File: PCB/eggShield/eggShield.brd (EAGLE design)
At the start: 100 x 80 mm, 35 parts, among them IC10 MCP601OT, IC3 LM339D, IC6 MCP601OT, IC7 MCP601OT

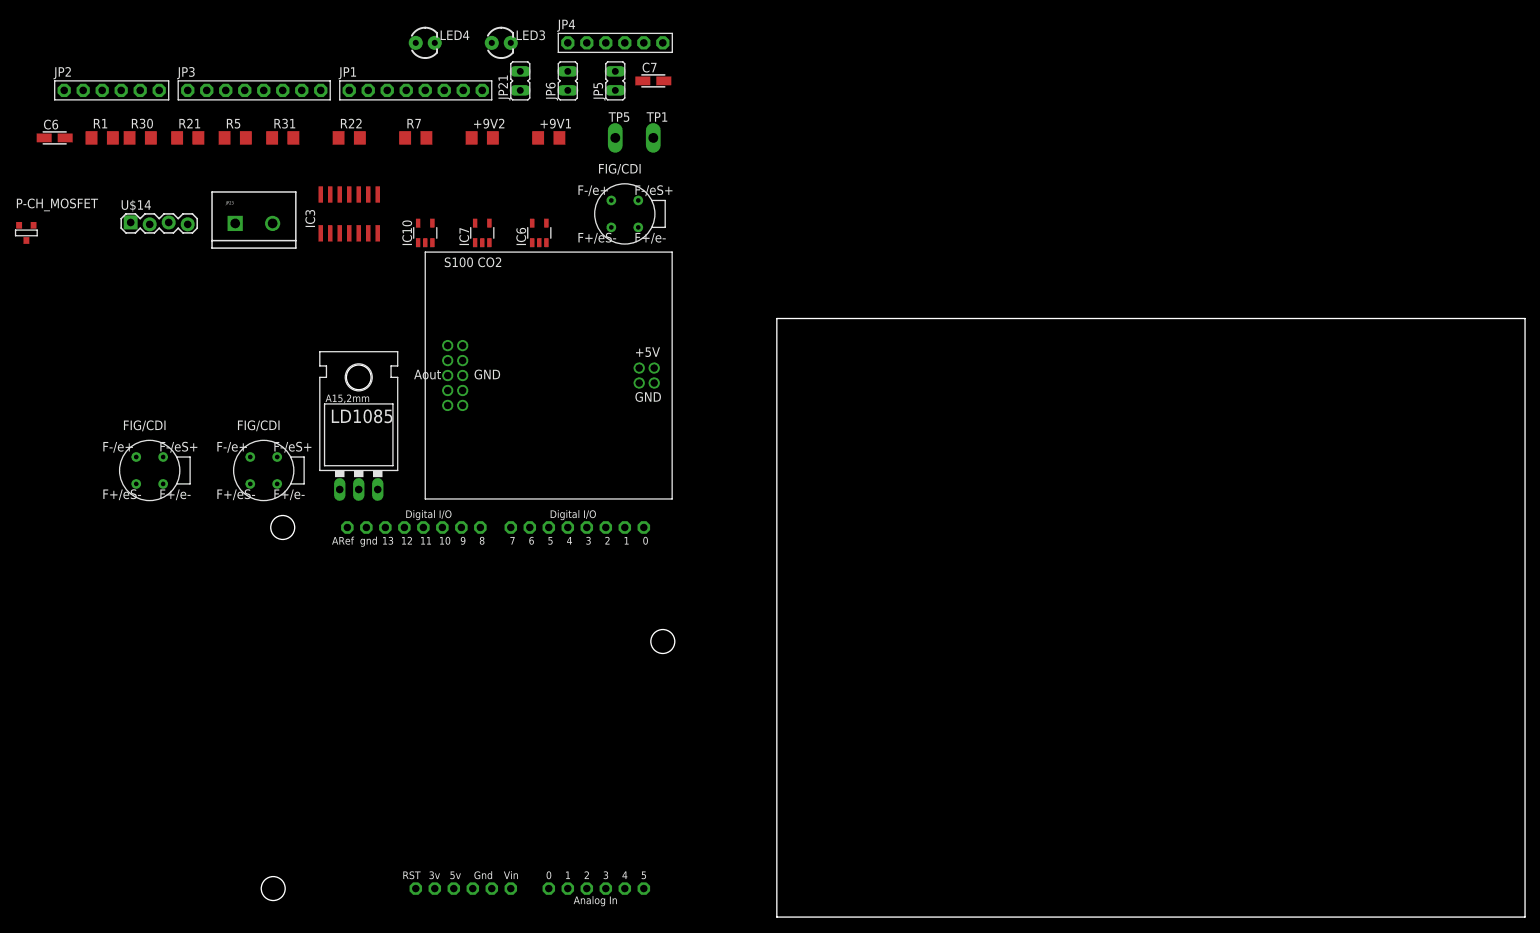
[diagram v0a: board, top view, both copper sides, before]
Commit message: added .brd, cleaned up
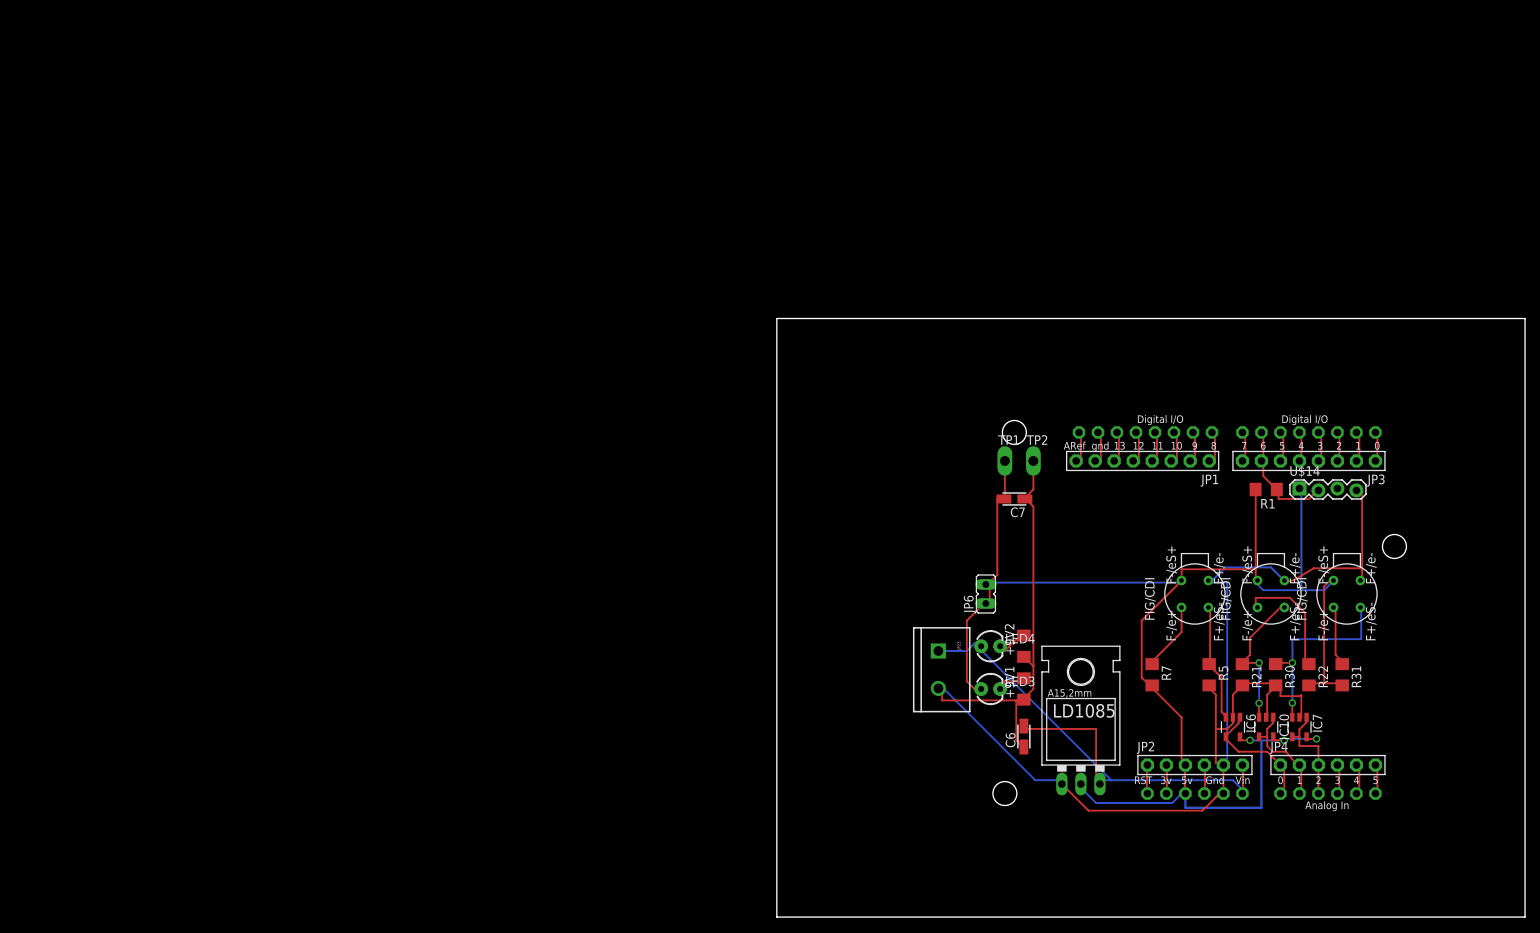
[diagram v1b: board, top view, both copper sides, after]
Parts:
- removed IC3: LM339D, linear:SO14
- removed JP21, JP5: (no value), jumper:JP1
- removed P-CH_MOSFET: ZXM61P02FCT, zetex:SOT-23
- removed TP5: TPPAD1-13Y, testpad:P1-13Y
- removed U$6: S100CO2, ricardo:S100CO2
- added TP2: TPPAD1-13Y, testpad:P1-13Y
- moved JP2 170.6 mm to (55.9, 20.3)
- moved R30 167.9 mm to (66.7, 32.4), turned to 270 degrees
- moved R1 162.5 mm to (65.4, 57.1), turned to 180 degrees
- moved U$9 160.9 mm to (76.2, 43.2), turned to 90 degrees
- moved U$14 160.2 mm to (69.8, 57.1)
- moved R31 158.7 mm to (75.6, 32.4), turned to 270 degrees
- moved R21 158.2 mm to (62.2, 32.4), turned to 270 degrees
- moved C6 152.3 mm to (33.0, 24.1), turned to 90 degrees
- moved JP3 149.4 mm to (71.1, 61.0), turned to 180 degrees
- moved R5 148.6 mm to (57.8, 32.4), turned to 270 degrees
- moved R22 147.0 mm to (71.1, 32.4), turned to 270 degrees
- moved JP4 135.6 mm to (73.7, 20.3)
- moved IC10 130.4 mm to (65.4, 25.4), turned to 180 degrees
- moved IC7 127.6 mm to (69.8, 25.4), turned to 180 degrees
- moved NO2 125.6 mm to (55.9, 43.2), turned to 90 degrees
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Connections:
- removed net A5: JP21.2, U$6.AOUT
- removed net D5: P-CH_MOSFET.3
- removed net N$49: P-CH_MOSFET.2, U$6.+5V1, U$6.+5V2
- net +9V: no longer IC3.3, JP5.1, JP5.2
- net GND: now also TP2.TP; no longer IC3.12, JP21.1, TP5.TP, U$6.GND2, U$6.GND9
- net V+: no longer P-CH_MOSFET.1
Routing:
- net V+: track 0.00 -> 216.2 mm, vias 0 -> 3
- net GND: track 0.00 -> 207.8 mm
- net +9V: track 0.00 -> 73.7 mm
- net N$55: track 0.00 -> 26.3 mm, vias 0 -> 2
- net N$47: track 0.00 -> 21.0 mm, vias 0 -> 2
- net N$52: track 0.00 -> 16.8 mm
- net N$50: track 0.00 -> 16.0 mm
- net A3: track 0.00 -> 15.8 mm
- net N$38: track 0.00 -> 15.8 mm
- net N$48: track 0.00 -> 14.6 mm
- net N$9: track 0.00 -> 14.1 mm
- net N$43: track 0.00 -> 9.17 mm
- net N$45: track 0.00 -> 8.03 mm
- net N$29: track 0.00 -> 4.71 mm
- net N$27: track 0.00 -> 4.71 mm
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
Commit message: cleaned board
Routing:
- net N$9: track 14.1 -> 12.6 mm
- net N$52: track 16.8 -> 17.8 mm
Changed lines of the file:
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@@
 <wire x1="22.352" y1="30.48" x2="21.59" y2="30.56" width="0.254" layer="16"/>
 <wire x1="37.592" y1="18.288" x2="38.1" y2="17.78" width="0.254" layer="16"/>
-<wire x1="56.896" y1="14.224" x2="58.674" y2="16.002" width="0.254" layer="1"/>
-<wire x1="58.674" y1="16.002" x2="58.928" y2="16.256" width="0.254" layer="1"/>
-<wire x1="41.656" y1="14.224" x2="56.896" y2="14.224" width="0.254" layer="1"/>
-<wire x1="38.1" y1="17.78" x2="41.656" y2="14.224" width="0.254" layer="1"/>
-<wire x1="58.928" y1="16.256" x2="59.69" y2="16.51" width="0.254" layer="1"/>
+<wire x1="59.436" y1="15.1765" x2="59.6265" y2="16.002" width="0.254" layer="1"/>
+<wire x1="59.6265" y1="16.002" x2="59.563" y2="16.256" width="0.254" layer="1"/>
+<wire x1="39.116" y1="15.1765" x2="59.436" y2="15.1765" width="0.254" layer="1"/>
+<wire x1="38.1" y1="17.78" x2="39.116" y2="15.1765" width="0.254" layer="1"/>
+<wire x1="59.563" y1="16.256" x2="59.69" y2="16.51" width="0.254" layer="1"/>
 <wire x1="60.96" y1="29.718" x2="60.96" y2="26.706" width="0.254" layer="1"/>
 <wire x1="61.722" y1="30.48" x2="60.96" y2="29.718" width="0.254" layer="1"/>
@@
 <wire x1="33.528" y1="29.718" x2="33.02" y2="29.058" width="0.254" layer="1"/>
 <wire x1="58.674" y1="29.718" x2="57.912" y2="30.48" width="0.254" layer="1"/>
-<wire x1="58.674" y1="16.002" x2="59.69" y2="16.51" width="0.254" layer="1"/>
+<wire x1="59.6265" y1="16.002" x2="59.69" y2="16.51" width="0.254" layer="1"/>
 <wire x1="59.69" y1="16.51" x2="59.69" y2="20.574" width="0.254" layer="1"/>
 <wire x1="59.69" y1="20.574" x2="59.436" y2="20.574" width="0.254" layer="1"/>
@@
 <wire x1="60.198" y1="24.384" x2="60.01" y2="24.094" width="0.254" layer="1"/>
 <wire x1="61.722" y1="26.67" x2="61.91" y2="26.706" width="0.254" layer="1"/>
-<wire x1="61.722" y1="22.098" x2="60.198" y2="23.622" width="0.254" layer="1"/>
-<wire x1="65.532" y1="22.098" x2="61.722" y2="22.098" width="0.254" layer="1"/>
-<wire x1="67.31" y1="20.32" x2="65.532" y2="22.098" width="0.254" layer="1"/>
+<wire x1="60.1345" y1="21.7805" x2="60.198" y2="23.622" width="0.254" layer="1"/>
+<wire x1="65.532" y1="21.7805" x2="60.1345" y2="21.7805" width="0.254" layer="1"/>
+<wire x1="67.31" y1="20.32" x2="65.532" y2="21.7805" width="0.254" layer="1"/>
 <wire x1="60.198" y1="23.622" x2="60.01" y2="24.094" width="0.254" layer="1"/>
 <wire x1="67.818" y1="19.812" x2="67.818" y2="16.764" width="0.254" layer="1"/>
@@
 <wire x1="65.532" y1="25.146" x2="66.294" y2="25.908" width="0.254" layer="1"/>
 <wire x1="65.532" y1="22.86" x2="65.532" y2="25.146" width="0.254" layer="1"/>
-<wire x1="66.294" y1="22.098" x2="65.532" y2="22.86" width="0.254" layer="1"/>
-<wire x1="68.072" y1="22.098" x2="66.294" y2="22.098" width="0.254" layer="1"/>
-<wire x1="69.342" y1="20.574" x2="68.072" y2="22.098" width="0.254" layer="1"/>
+<wire x1="65.659" y1="22.733" x2="65.532" y2="22.86" width="0.254" layer="1"/>
+<wire x1="67.437" y1="22.733" x2="65.659" y2="22.733" width="0.254" layer="1"/>
+<wire x1="69.977" y1="20.2565" x2="67.437" y2="22.733" width="0.254" layer="1"/>
 <wire x1="66.294" y1="26.67" x2="66.355" y2="26.706" width="0.254" layer="1"/>
-<wire x1="69.342" y1="20.574" x2="69.85" y2="20.32" width="0.254" layer="1"/>
+<wire x1="69.977" y1="20.2565" x2="69.85" y2="20.32" width="0.254" layer="1"/>
 <wire x1="70.104" y1="19.812" x2="70.104" y2="16.764" width="0.254" layer="1"/>
 <wire x1="70.104" y1="16.764" x2="69.85" y2="16.51" width="0.254" layer="1"/>
@@
 <wire x1="68.9" y1="24.094" x2="69.85" y2="24.094" width="0.254" layer="1"/>
 <wire x1="69.85" y1="24.094" x2="69.85" y2="22.86" width="0.254" layer="1"/>
-<wire x1="69.85" y1="22.86" x2="72.39" y2="22.86" width="0.254" layer="1"/>
-<wire x1="72.39" y1="22.86" x2="72.39" y2="20.32" width="0.254" layer="1"/>
+<wire x1="69.85" y1="22.86" x2="72.39" y2="20.32" width="0.254" layer="1"/>
 </signal>
 <signal name="N$10">

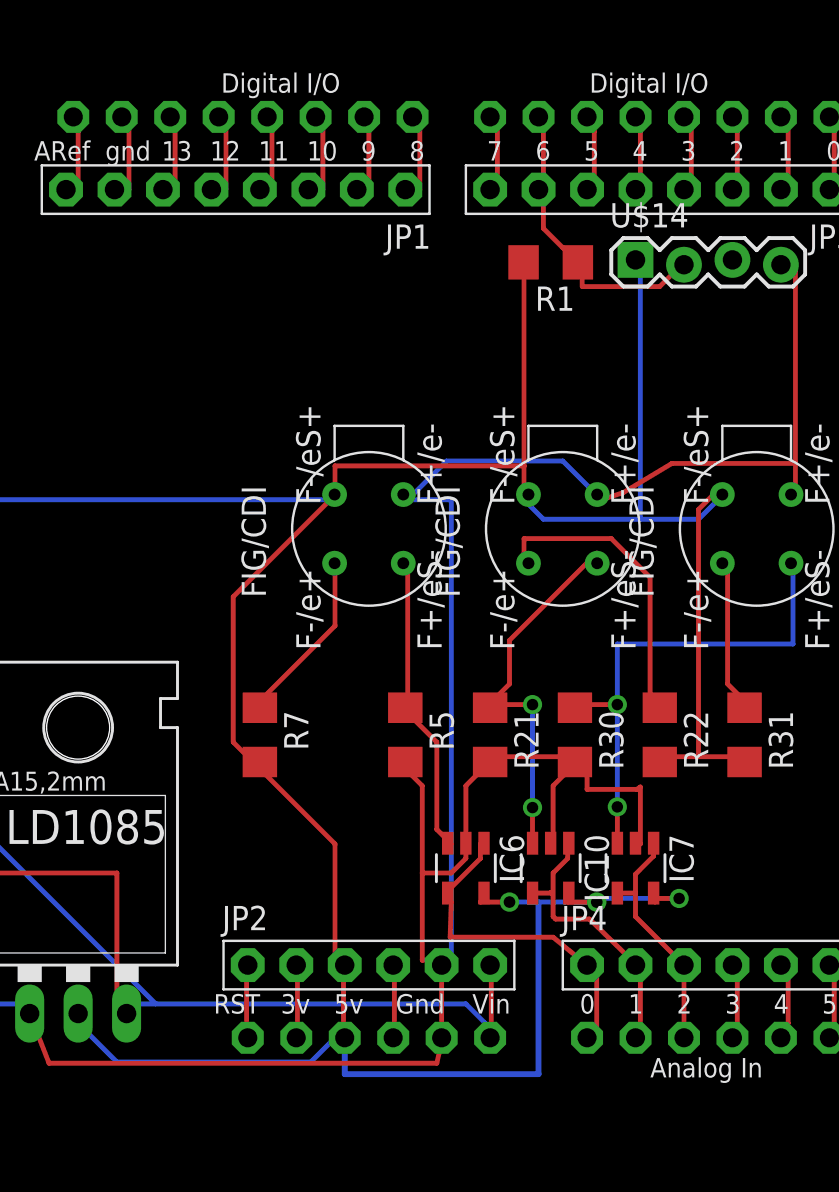
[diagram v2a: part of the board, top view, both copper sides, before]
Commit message: fixed RHT pin
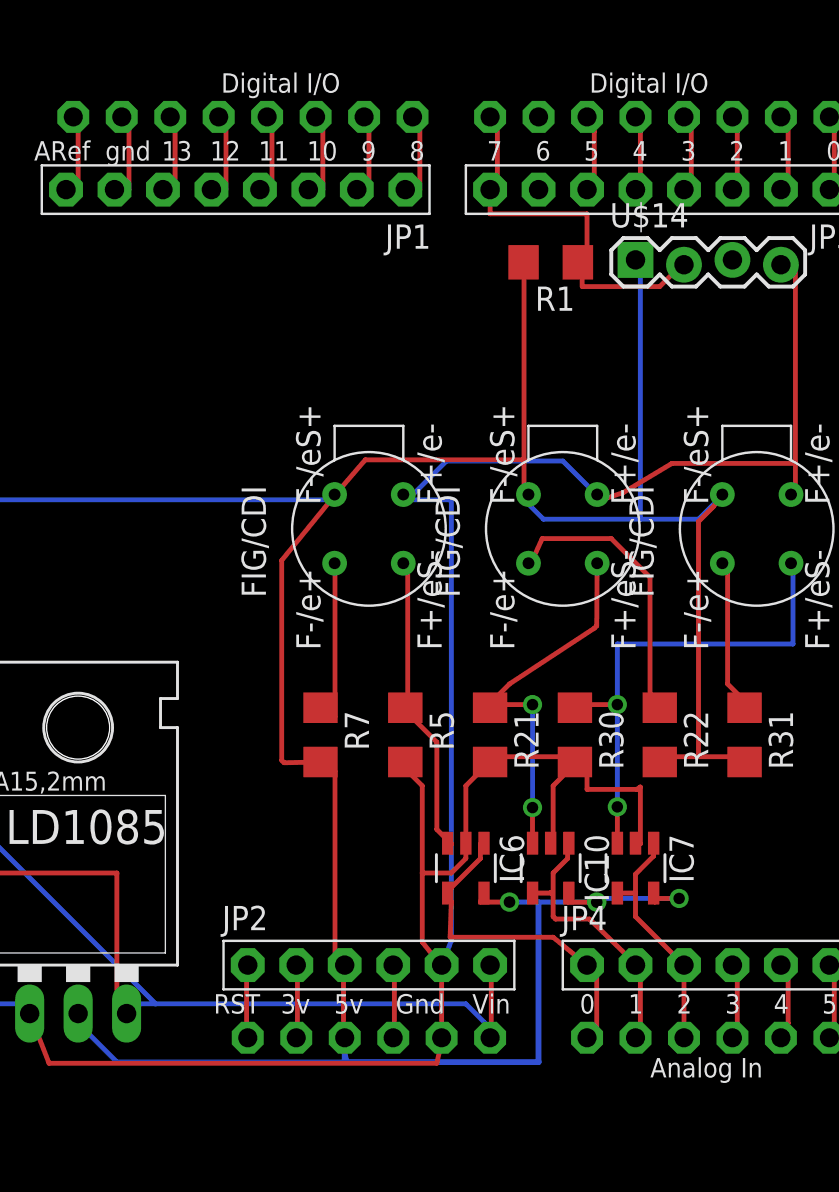
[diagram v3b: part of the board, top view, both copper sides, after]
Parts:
- moved R7 3.18 mm to (53.3, 32.4)
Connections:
- removed net N$21: JP3.8, U$2.D7
- new net N$5: JP3.7, U$2.D6
- net A3: now also JP3.8, U$2.D7; no longer JP3.7, U$2.D6
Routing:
- net A3: track 15.8 -> 20.8 mm
- net N$21: track 4.33 -> 0.00 mm
- net V+: track 216.2 -> 213.8 mm
- net GND: track 207.7 -> 206.8 mm
- net N$38: track 15.8 -> 15.2 mm
- net N$47: track 21.0 -> 20.5 mm

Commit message: cleaned up a bit
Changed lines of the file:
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@@
 <wire x1="59.436" y1="15.1765" x2="59.6265" y2="16.002" width="0.254" layer="1"/>
 <wire x1="59.6265" y1="16.002" x2="59.563" y2="16.256" width="0.254" layer="1"/>
-<wire x1="39.116" y1="15.1765" x2="59.436" y2="15.1765" width="0.254" layer="1"/>
-<wire x1="38.1" y1="17.78" x2="39.116" y2="15.1765" width="0.254" layer="1"/>
+<wire x1="39.751" y1="15.1765" x2="59.436" y2="15.1765" width="0.254" layer="1"/>
+<wire x1="38.1" y1="17.78" x2="39.751" y2="15.1765" width="0.254" layer="1"/>
 <wire x1="59.563" y1="16.256" x2="59.69" y2="16.51" width="0.254" layer="1"/>
 <wire x1="60.96" y1="29.718" x2="60.96" y2="26.706" width="0.254" layer="1"/>
@@
 <wire x1="62.611" y1="60.96" x2="62.23" y2="60.96" width="0.254" layer="1"/>
 <wire x1="66.827" y1="57.15" x2="67.31" y2="57.15" width="0.254" layer="1"/>
-<wire x1="67.31" y1="57.15" x2="67.31" y2="59.69" width="0.254" layer="1"/>
-<wire x1="67.31" y1="59.69" x2="62.23" y2="59.69" width="0.254" layer="1"/>
-<wire x1="62.23" y1="59.69" x2="62.23" y2="60.96" width="0.254" layer="1"/>
+<wire x1="67.31" y1="57.15" x2="67.31" y2="59.055" width="0.254" layer="1"/>
+<wire x1="67.31" y1="59.055" x2="62.23" y2="59.055" width="0.254" layer="1"/>
+<wire x1="62.23" y1="59.055" x2="62.23" y2="60.96" width="0.254" layer="1"/>
 <wire x1="62.23" y1="60.96" x2="62.611" y2="60.96" width="0" layer="19" extent="1-16"/>
 </signal>
